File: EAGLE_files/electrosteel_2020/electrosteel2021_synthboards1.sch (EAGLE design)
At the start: 143 parts, among them IC1 OPA4344E, J1 4P-2.0, J2 4P-2.0, J3 4P-2.0, J36 4P-2.0, J4 4P-2.0, U1 MAX11615EEE+, U15 R-78E5.0-1.0, U17 R-78E5.0-1.0, U2 R-78E5.0-1.0, U20 TCA9548APWR, X6 2520-, X7 2516-

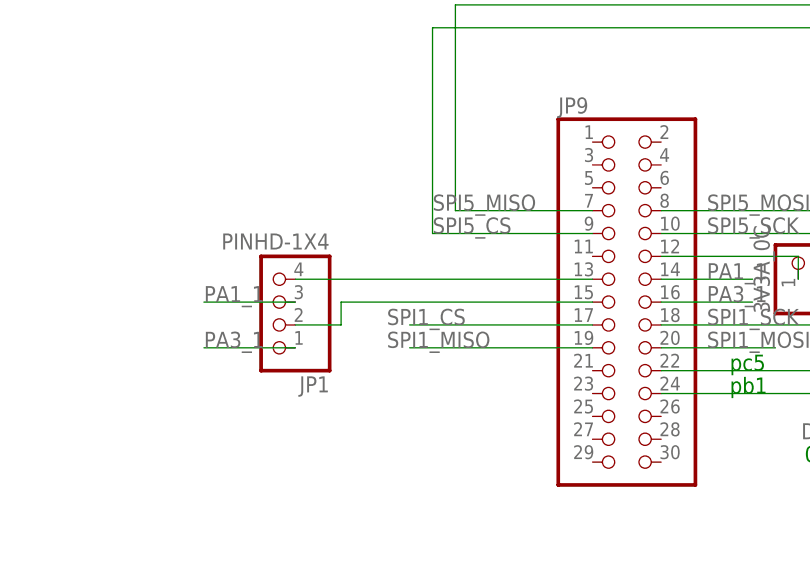
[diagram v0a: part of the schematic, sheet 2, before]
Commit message: working electrosteel, doesnt take in new patches but reads electrobass patches off sdcard
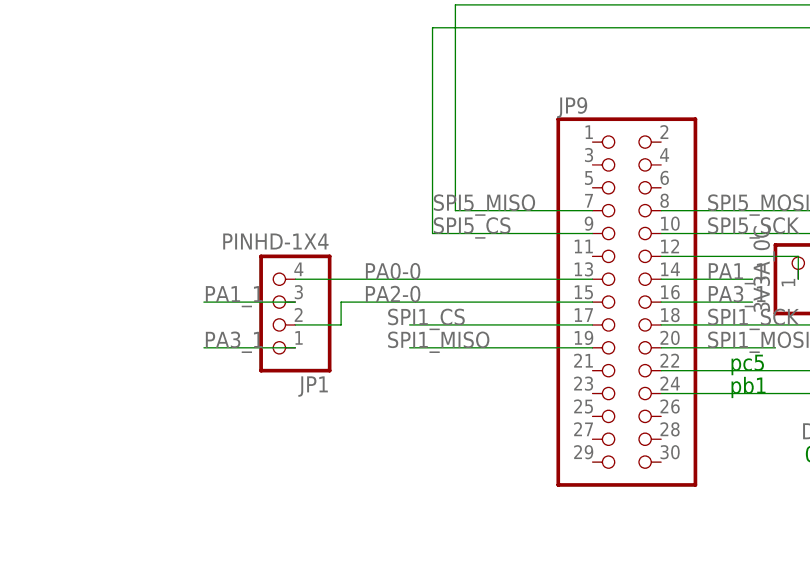
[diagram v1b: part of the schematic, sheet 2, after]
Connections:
- net N$298 renamed PA0-0
- net N$300 renamed PA2-0
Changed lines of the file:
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@@
 </segment>
 </net>
-<net name="N$298" class="0">
+<net name="PA0-0" class="0">
 <segment>
 <pinref part="JP9" gate="A" pin="13"/>
 <pinref part="JP1" gate="A" pin="4"/>
 <wire x1="81.28" y1="17.78" x2="48.26" y2="17.78" width="0.1524" layer="91"/>
+<label x="55.88" y="17.78" size="1.778" layer="95"/>
 </segment>
 </net>
@@
 </segment>
 </net>
-<net name="N$300" class="0">
+<net name="PA2-0" class="0">
 <segment>
 <pinref part="JP9" gate="A" pin="15"/>
@@
 <pinref part="JP1" gate="A" pin="2"/>
 <wire x1="53.34" y1="12.7" x2="48.26" y2="12.7" width="0.1524" layer="91"/>
+<label x="55.88" y="15.24" size="1.778" layer="95"/>
 </segment>
 </net>
